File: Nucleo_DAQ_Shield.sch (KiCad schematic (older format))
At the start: 32 parts, among them J1 CONN_01X06, J2 CONN_01X06, J3 CONN_01X02, J4 CONN_01X02, J6 CONN_COAXIAL, J7 CONN_01X02, U1 4050, U10 ST_Nucleo144_F746ZG_CN10, U2 TL072, U3 LM7805CT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

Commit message: Added through hold Schottky diode as an alternative to SOD-123 Schottky diode
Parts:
- removed D1: D_Schottky, Diodes_SMD:D_SOD-123, symbol D_Schottky
- added D1: SD103 SOD-123, Diodes_SMD:D_SOD-123, symbol D_Schottky_Small
- added D3: SD103 DO-35, Diodes_THT:D_DO-35_SOD27_P7.62mm_Horizontal, symbol D_Schottky_Small
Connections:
- wire segments 48 -> 51
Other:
- note added: "Jumper enables overvoltage protection\n with the Schottky diode\nOnly solder one of the diodes shown"
- note removed: "Jumper enables overvoltage protection\n with the Schottky diode"
- moved on the sheet: J6, R1, R5, R6
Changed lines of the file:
@@
 L CONN_COAXIAL J6
 U 1 1 59542D8D
-P 5050 5900
-F 0 "J6" H 5060 6020 50  0000 C CNN
-F 1 "CONN_COAXIAL" V 5165 5900 50  0000 C CNN
-F 2 "custom:SMA_uxcell" H 5050 5900 50  0001 C CNN
-F 3 "" H 5050 5900 50  0001 C CNN
-	1    5050 5900
+P 4850 5900
+F 0 "J6" H 4860 6020 50  0000 C CNN
+F 1 "CONN_COAXIAL" V 4965 5900 50  0000 C CNN
+F 2 "custom:SMA_uxcell" H 4850 5900 50  0001 C CNN
+F 3 "" H 4850 5900 50  0001 C CNN
+	1    4850 5900
 	-1   0    0    -1
 $EndComp
@@
 L GNDA #PWR010
 U 1 1 59543B89
-P 5050 6100
-F 0 "#PWR010" H 5050 5850 50  0001 C CNN
-F 1 "GNDA" H 5050 5950 50  0000 C CNN
-F 2 "" H 5050 6100 50  0001 C CNN
-F 3 "" H 5050 6100 50  0001 C CNN
-	1    5050 6100
+P 4850 6100
+F 0 "#PWR010" H 4850 5850 50  0001 C CNN
+F 1 "GNDA" H 4850 5950 50  0000 C CNN
+F 2 "" H 4850 6100 50  0001 C CNN
+F 3 "" H 4850 6100 50  0001 C CNN
+	1    4850 6100
 	1    0    0    -1
 $EndComp
@@
 Nucleo connectors
 $Comp
-L D_Schottky D1
-U 1 1 595D9361
-P 6100 5650
-F 0 "D1" H 6100 5750 50  0000 C CNN
-F 1 "D_Schottky" H 6100 5550 50  0000 C CNN
-F 2 "Diodes_SMD:D_SOD-123" H 6100 5650 50  0001 C CNN
-F 3 "" H 6100 5650 50  0001 C CNN
-	1    6100 5650
-	0    1    1    0
-$EndComp
-$Comp
 L Jumper_NC_Small JP3
 U 1 1 595D9DFC
@@
 L R_Small R1
 U 1 1 595DA3C3
-P 5800 5900
-F 0 "R1" H 5830 5920 50  0000 L CNN
-F 1 "100" H 5830 5860 50  0000 L CNN
-F 2 "Resistors_SMD:R_0805" H 5800 5900 50  0001 C CNN
-F 3 "" H 5800 5900 50  0001 C CNN
-	1    5800 5900
+P 5600 5900
+F 0 "R1" H 5630 5920 50  0000 L CNN
+F 1 "100" H 5630 5860 50  0000 L CNN
+F 2 "Resistors_SMD:R_0805" H 5600 5900 50  0001 C CNN
+F 3 "" H 5600 5900 50  0001 C CNN
+	1    5600 5900
 	0    1    1    0
 $EndComp
 Text Notes 5650 5350 0    30   ~ 0
-Jumper enables overvoltage protection\n with the Schottky diode
+Jumper enables overvoltage protection\n with the Schottky diode\nOnly solder one of the diodes shown
 Text Notes 750  2050 0    60   ~ 0
 Motor and encoder interface
-Text Notes 5200 6350 0    30   ~ 0
+Text Notes 5000 6350 0    30   ~ 0
 50 Ohm termination resistor
 Text Notes 1800 3650 0    30   ~ 0
@@
 	600  5100 600  2100
 Wire Notes Line
-	4800 6500 4800 5200
-Wire Wire Line
-	5200 5900 5700 5900
-Connection ~ 6100 5900
-Wire Wire Line
-	6100 5800 6100 5900
-Wire Wire Line
-	5900 5900 6500 5900
-Wire Wire Line
-	6100 5500 6300 5500
+	4600 6500 4600 5200
+Wire Wire Line
+	5000 5900 5500 5900
+Wire Wire Line
+	5700 5900 6500 5900
 Connection ~ 6700 5500
 Wire Wire Line
@@
 Connection ~ 2100 1000
 Wire Notes Line
-	4800 6500 8200 6500
+	4600 6500 8200 6500
 Wire Notes Line
 	8200 6500 8200 5200
 Wire Notes Line
-	8200 5200 4800 5200
+	8200 5200 4600 5200
 Connection ~ 7200 6000
 Wire Notes Line
@@
 L R_Small R6
 U 1 1 59654171
-P 5600 6000
-F 0 "R6" H 5630 6020 50  0000 L CNN
-F 1 "100" H 5630 5960 50  0000 L CNN
-F 2 "Resistors_SMD:R_0805" H 5600 6000 50  0001 C CNN
-F 3 "" H 5600 6000 50  0001 C CNN
-	1    5600 6000
-	-1   0    0    1
-$EndComp
-$Comp
-L R_Small R5
-U 1 1 596541F7
 P 5400 6000
-F 0 "R5" H 5430 6020 50  0000 L CNN
+F 0 "R6" H 5430 6020 50  0000 L CNN
 F 1 "100" H 5430 5960 50  0000 L CNN
 F 2 "Resistors_SMD:R_0805" H 5400 6000 50  0001 C CNN
@@
 $EndComp
 $Comp
+L R_Small R5
+U 1 1 596541F7
+P 5200 6000
+F 0 "R5" H 5230 6020 50  0000 L CNN
+F 1 "100" H 5230 5960 50  0000 L CNN
+F 2 "Resistors_SMD:R_0805" H 5200 6000 50  0001 C CNN
+F 3 "" H 5200 6000 50  0001 C CNN
+	1    5200 6000
+	-1   0    0    1
+$EndComp
+$Comp
 L GNDA #PWR048
 U 1 1 5965449B
-P 5600 6100
-F 0 "#PWR048" H 5600 5850 50  0001 C CNN
-F 1 "GNDA" H 5600 5950 50  0000 C CNN
-F 2 "" H 5600 6100 50  0001 C CNN
-F 3 "" H 5600 6100 50  0001 C CNN
-	1    5600 6100
-	1    0    0    -1
-$EndComp
-$Comp
-L GNDA #PWR049
-U 1 1 59654512
 P 5400 6100
-F 0 "#PWR049" H 5400 5850 50  0001 C CNN
+F 0 "#PWR048" H 5400 5850 50  0001 C CNN
 F 1 "GNDA" H 5400 5950 50  0000 C CNN
 F 2 "" H 5400 6100 50  0001 C CNN
@@
 	1    0    0    -1
 $EndComp
-Connection ~ 5600 5900
+$Comp
+L GNDA #PWR049
+U 1 1 59654512
+P 5200 6100
+F 0 "#PWR049" H 5200 5850 50  0001 C CNN
+F 1 "GNDA" H 5200 5950 50  0000 C CNN
+F 2 "" H 5200 6100 50  0001 C CNN
+F 3 "" H 5200 6100 50  0001 C CNN
+	1    5200 6100
+	1    0    0    -1
+$EndComp
 Connection ~ 5400 5900
+Connection ~ 5200 5900
 NoConn ~ 6700 1100
 NoConn ~ 6700 1200
@@
 NoConn ~ 10200 4200
 NoConn ~ 1100 4000
-Text Notes 5000 5700 0    30   ~ 0
+Text Notes 4800 5700 0    30   ~ 0
 SMA connector
 $Comp
@@
 	1    0    0    -1
 $EndComp
+$Comp
+L D_Schottky_Small D1
+U 1 1 5965AAB6
+P 6150 5700
+F 0 "D1" H 6100 5780 50  0000 L CNN
+F 1 "SD103 SOD-123" H 5870 5620 30  0000 L CNN
+F 2 "Diodes_SMD:D_SOD-123" V 6150 5700 50  0001 C CNN
+F 3 "" V 6150 5700 50  0001 C CNN
+	1    6150 5700
+	0    1    1    0
+$EndComp
+Wire Wire Line
+	6150 5800 6150 5900
+Connection ~ 6150 5900
+Wire Wire Line
+	6150 5600 6150 5500
+Wire Wire Line
+	5900 5500 6300 5500
+$Comp
+L D_Schottky_Small D3
+U 1 1 5965B94C
+P 5900 5700
+F 0 "D3" H 5850 5780 50  0000 L CNN
+F 1 "SD103 DO-35" H 5620 5620 30  0000 L CNN
+F 2 "Diodes_THT:D_DO-35_SOD27_P7.62mm_Horizontal" V 5900 5700 50  0001 C CNN
+F 3 "" V 5900 5700 50  0001 C CNN
+	1    5900 5700
+	0    1    1    0
+$EndComp
+Wire Wire Line
+	5900 5600 5900 5500
+Connection ~ 6150 5500
+Wire Wire Line
+	5900 5800 5900 5900
+Connection ~ 5900 5900
 $EndSCHEMATC

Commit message: Nucleo DAQ Shield v1.2
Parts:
- U3: value LM7805CT -> L78L05
- U5: footprint Housings_SOIC:SOIC-8_3.9x4.9mm_Pitch1.27mm -> custom:SOIC-8_PowerPad
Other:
- note added: "3.3V 300mA regulator\nSOT-23-5 package"
- note added: "5V LDO regulator 100mA\nTO-92 package"
- note removed: "3.3V 300mA regulator"
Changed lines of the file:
@@
 Title "Nucleo DAQ Shield"
 Date "2017-07-11"
-Rev "v1.0"
+Rev "v1.2"
 Comp "Columbia University - Creative Machines Lab"
 Comment1 ""
@@
 Vbat
 Text Notes 5100 800  0    30   ~ 0
-3.3V 300mA regulator
+3.3V 300mA regulator\nSOT-23-5 package
 $Comp
 L GND #PWR019
@@
 F 0 "U5" H 4900 4025 60  0000 C CNN
 F 1 "DRV8881" H 4900 3900 60  0000 C CNN
-F 2 "Housings_SOIC:SOIC-8_3.9x4.9mm_Pitch1.27mm" H 4900 3550 60  0001 C CNN
+F 2 "custom:SOIC-8_PowerPad" H 4900 3550 60  0001 C CNN
 F 3 "" H 4900 3550 60  0001 C CNN
 	1    4900 3550
@@
 P 3200 1050
 F 0 "U3" H 3000 1250 50  0000 C CNN
-F 1 "LM7805CT" H 3200 1250 50  0000 L CNN
+F 1 "L78L05" H 3200 1250 50  0000 L CNN
 F 2 "TO_SOT_Packages_THT:TO-92_Inline_Narrow_Oval" H 3200 1150 50  0001 C CIN
 F 3 "" H 3200 1050 50  0001 C CNN
@@
 	5900 5800 5900 5900
 Connection ~ 5900 5900
+Text Notes 2950 800  0    30   ~ 0
+5V LDO regulator 100mA\nTO-92 package
 $EndSCHEMATC

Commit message: Swapped out TO-92 footprint to make it larger; refined separation between AGND and DGND
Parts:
- U3: footprint TO_SOT_Packages_THT:TO-92_Inline_Narrow_Oval -> TO_SOT_Packages_THT:TO-92_Inline_Wide
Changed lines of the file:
@@
 F 0 "U3" H 3000 1250 50  0000 C CNN
 F 1 "L78L05" H 3200 1250 50  0000 L CNN
-F 2 "TO_SOT_Packages_THT:TO-92_Inline_Narrow_Oval" H 3200 1150 50  0001 C CIN
+F 2 "TO_SOT_Packages_THT:TO-92_Inline_Wide" H 3200 1150 50  0001 C CIN
 F 3 "" H 3200 1050 50  0001 C CNN
 	1    3200 1050

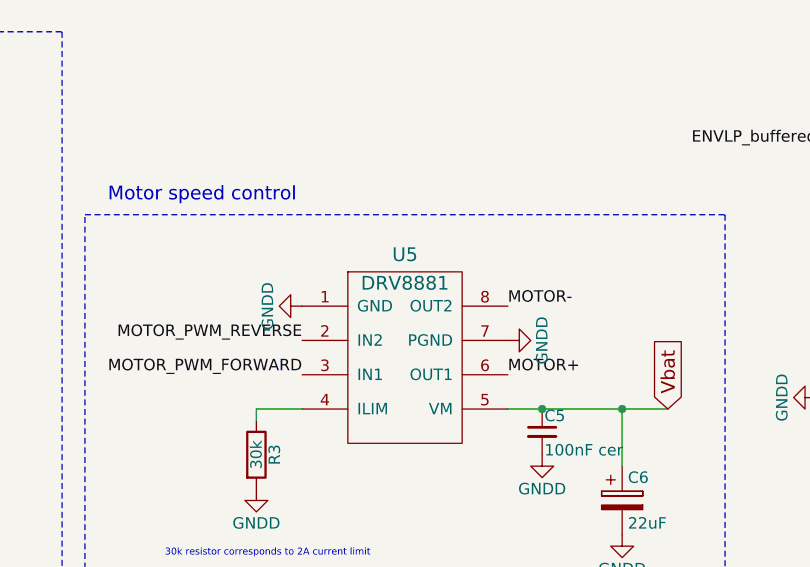
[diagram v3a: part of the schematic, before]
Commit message: BOM for Analog Frontend PCB v1.3
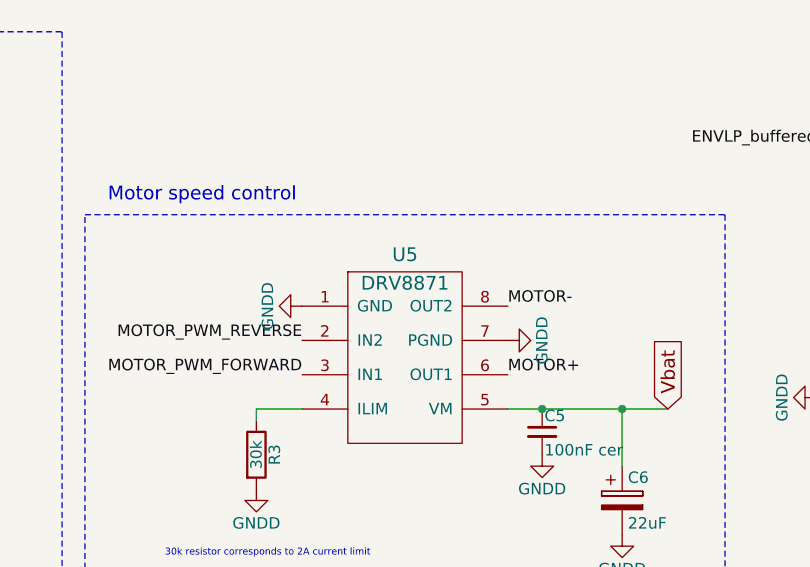
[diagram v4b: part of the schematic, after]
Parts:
- U5: value DRV8881 -> DRV8871
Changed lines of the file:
@@
 P 4900 3550
 F 0 "U5" H 4900 4025 60  0000 C CNN
-F 1 "DRV8881" H 4900 3900 60  0000 C CNN
+F 1 "DRV8871" H 4900 3900 60  0000 C CNN
 F 2 "custom:SOIC-8_PowerPad" H 4900 3550 60  0001 C CNN
 F 3 "" H 4900 3550 60  0001 C CNN

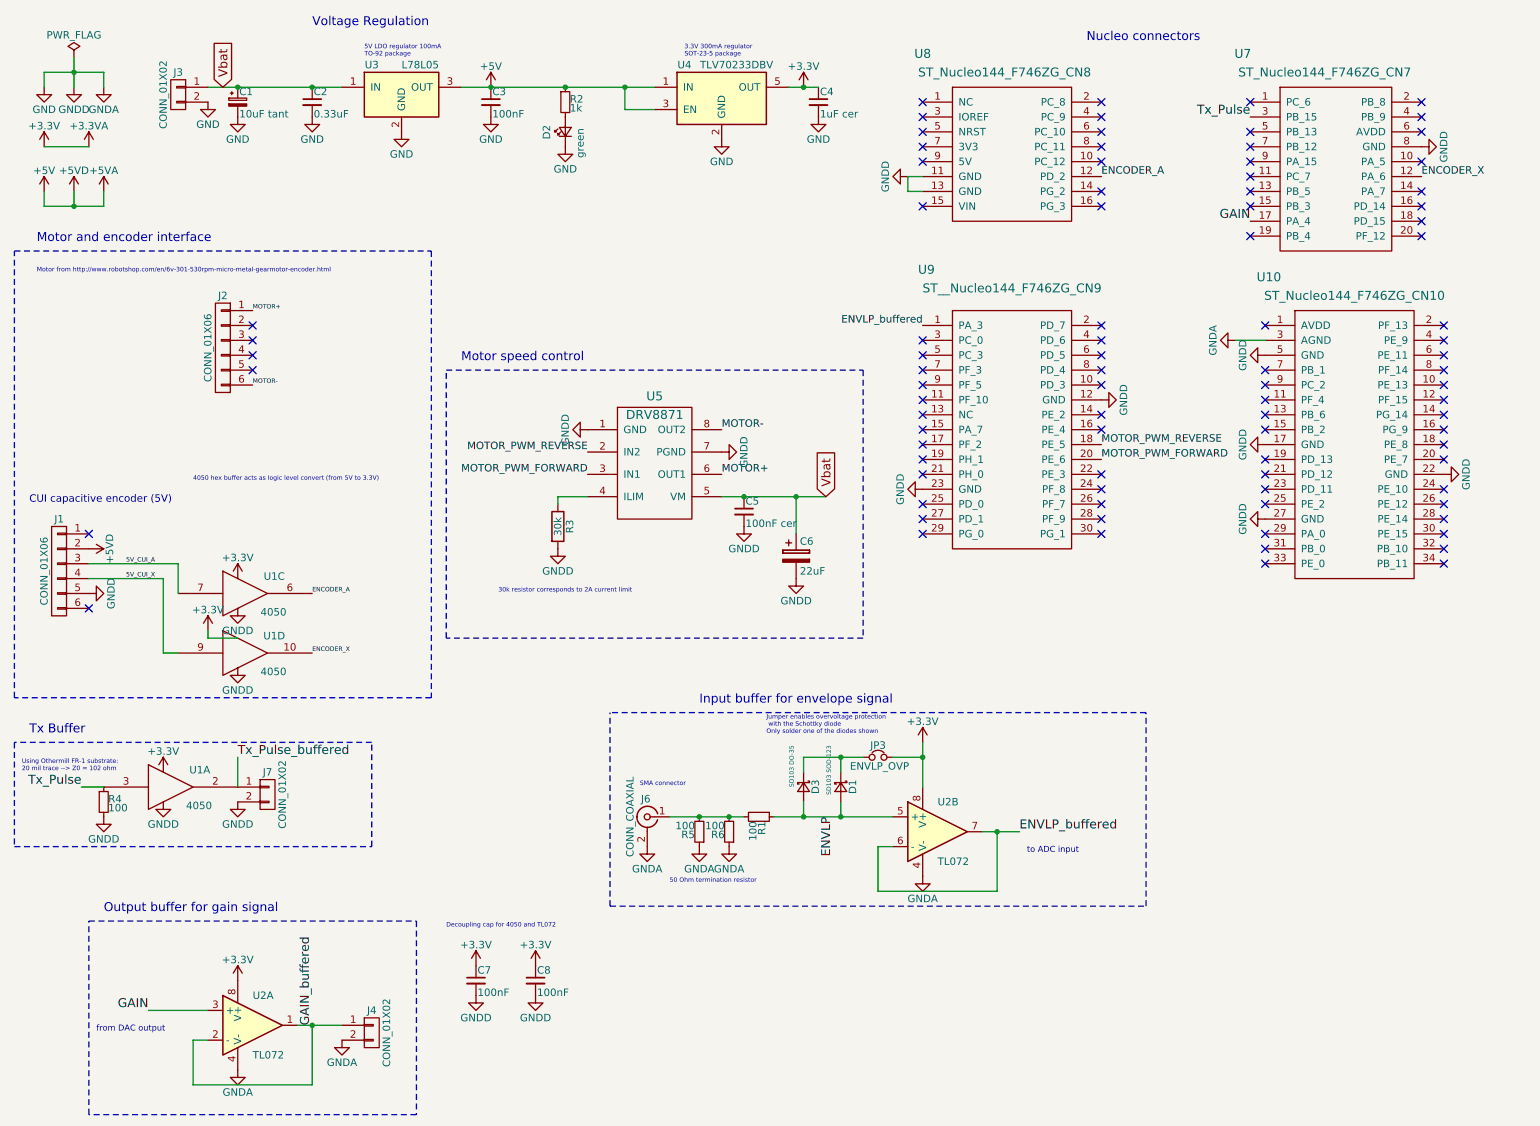
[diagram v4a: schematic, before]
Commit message: Analog BOM & Nucleo pins added
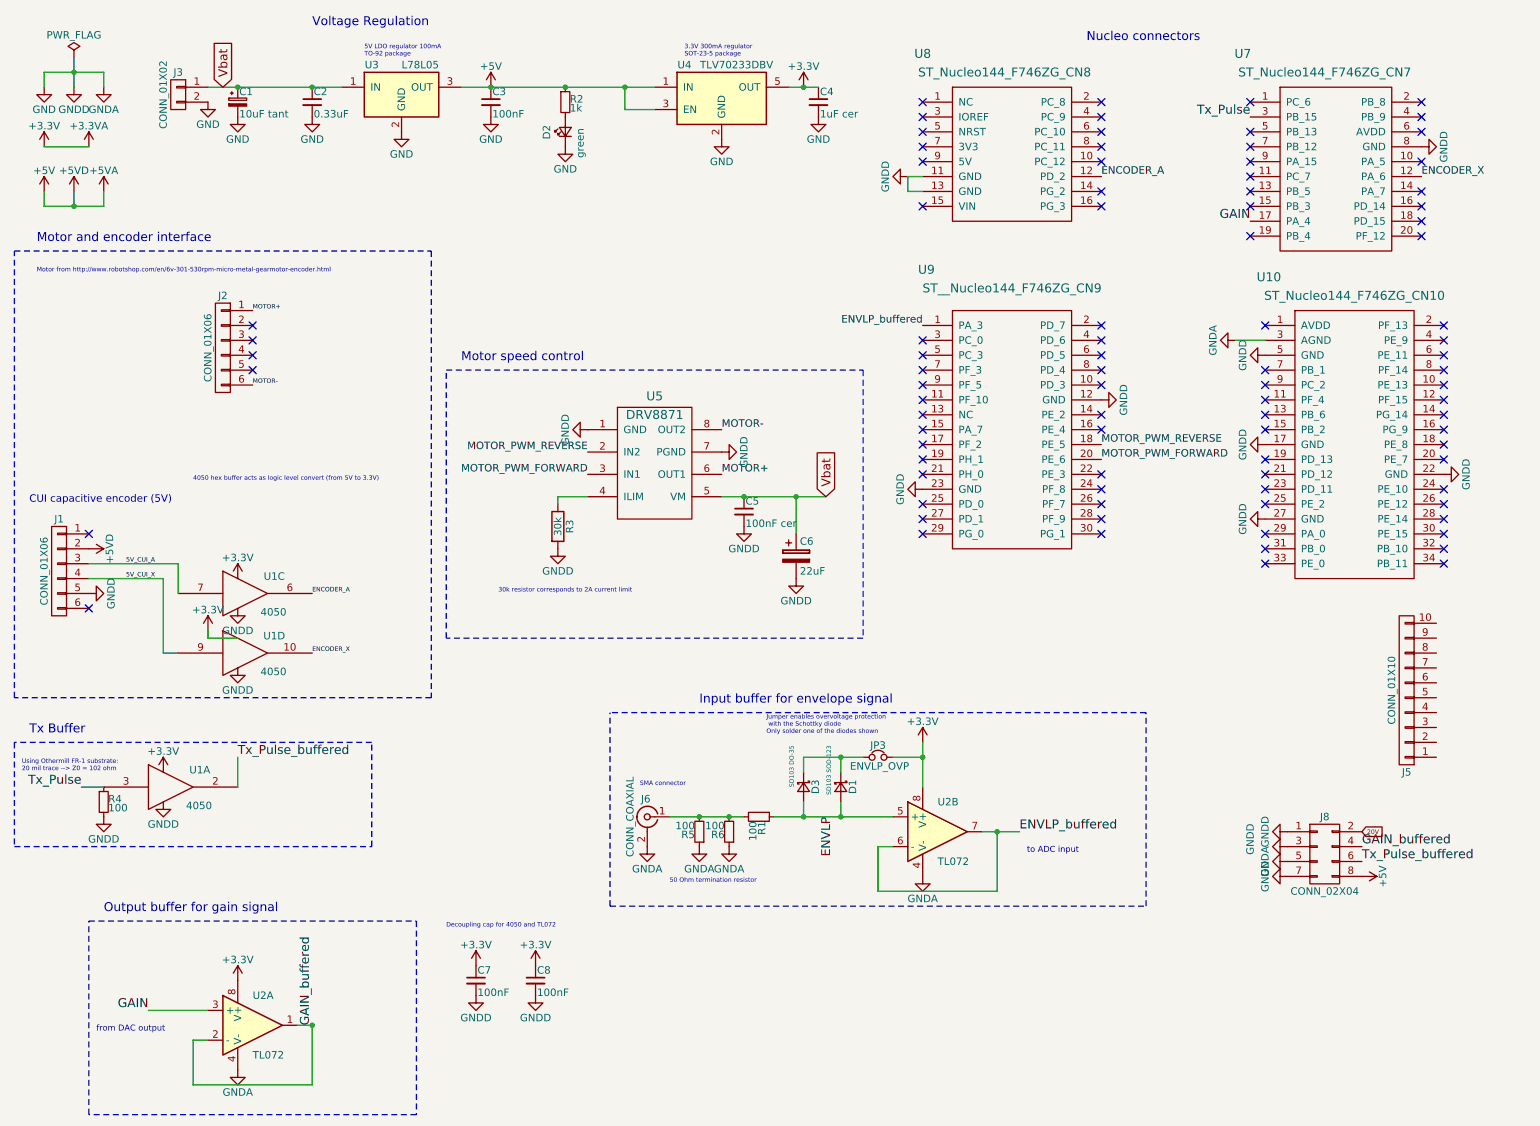
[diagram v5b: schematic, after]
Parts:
- removed J4, J7: CONN_01X02, Pin_Headers:Pin_Header_Straight_1x02_Pitch2.54mm, symbol CONN_01X02
- added J5: CONN_01X10, Pin_Headers:Pin_Header_Angled_1x10_Pitch2.54mm, symbol CONN_01X10
- added J8: CONN_02X04, Pin_Headers:Pin_Header_Straight_2x04_Pitch2.54mm, symbol CONN_02X04
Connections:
- net +5V: now also J8.8 (P8)
- net GAIN_buffered: now also J8.4 (P4)
- net GND: now also J8.1 (P1), J8.3 (P3), J8.5 (P5), J8.7 (P7)
- net Tx_Pulse_buffered: now also J8.6 (P6)
- new net 20V: J8.2 (P2)

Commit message: nucleo board updated
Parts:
- removed D3: SD103 DO-35, Diodes_THT:D_DO-35_SOD27_P7.62mm_Horizontal, symbol D_Schottky_Small
- removed J1: CONN_01X06, Pin_Headers:Pin_Header_Straight_1x06_Pitch2.54mm, symbol CONN_01X06
- added J1: CONN_01X05, Pin_Headers:Pin_Header_Straight_1x05_Pitch2.54mm, symbol CONN_01X05
- added J9: CONN_01X04, Pin_Headers:Pin_Header_Straight_1x04_Pitch2.54mm, symbol CONN_01X04
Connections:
- net +5V: now also J8.6 (P6), J1.4 (P4), J9.3 (P3); no longer J8.8 (P8)
- net 20V: now also J9.1 (P1)
- net 5V_CUI_A: now also J1.3 (P3)
- net 5V_CUI_X: now also J1.2 (P2)
- net GND: now also J1.1 (P1), J9.2 (P2), J9.4 (P4)
- net Tx_Pulse_buffered: now also J8.8 (P8); no longer J8.6 (P6)
- no-connect marks 89 -> 88
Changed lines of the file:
@@
 $EndComp
-$Comp
-L CONN_01X06 J1
-U 1 1 595D423B
-P 900 4250
-F 0 "J1" H 900 4600 50  0000 C CNN
-F 1 "CONN_01X06" V 1000 4250 50  0000 C CNN
-F 2 "Pin_Headers:Pin_Header_Straight_1x06_Pitch2.54mm" H 900 4250 50  0001 C CNN
-F 3 "" H 900 4250 50  0001 C CNN
-	1    900  4250
-	-1   0    0    -1
-$EndComp
-NoConn ~ 1100 4500
 $Comp
 L +5VD #PWR020
@@
 Wire Wire Line
 	6150 5600 6150 5500
-Wire Wire Line
-	5900 5500 6300 5500
-$Comp
-L D_Schottky_Small D3
-U 1 1 5965B94C
-P 5900 5700
-F 0 "D3" H 5850 5780 50  0000 L CNN
-F 1 "SD103 DO-35" H 5620 5620 30  0000 L CNN
-F 2 "Diodes_THT:D_DO-35_SOD27_P7.62mm_Horizontal" V 5900 5700 50  0001 C CNN
-F 3 "" V 5900 5700 50  0001 C CNN
-	1    5900 5700
-	0    1    1    0
-$EndComp
-Wire Wire Line
-	5900 5600 5900 5500
 Connection ~ 6150 5500
-Wire Wire Line
-	5900 5800 5900 5900
-Connection ~ 5900 5900
 Text Notes 2950 800  0    30   ~ 0
 5V LDO regulator 100mA\nTO-92 package
@@
 L +5V #PWR058
 U 1 1 59E8A941
-P 9650 6300
-F 0 "#PWR058" H 9650 6150 50  0001 C CNN
-F 1 "+5V" H 9650 6440 50  0000 C CNN
-F 2 "" H 9650 6300 50  0001 C CNN
-F 3 "" H 9650 6300 50  0001 C CNN
-	1    9650 6300
+P 9650 6200
+F 0 "#PWR058" H 9650 6050 50  0001 C CNN
+F 1 "+5V" H 9650 6340 50  0000 C CNN
+F 2 "" H 9650 6200 50  0001 C CNN
+F 3 "" H 9650 6200 50  0001 C CNN
+	1    9650 6200
 	0    1    1    0
 $EndComp
 Text GLabel 9650 6000 2    30   Input ~ 0
 20V
-Text Label 9650 6200 0    60   ~ 0
+Text Label 9650 6300 0    60   ~ 0
 Tx_Pulse_buffered
+Wire Wire Line
+	6150 5500 6300 5500
+$Comp
+L CONN_01X04 J9
+U 1 1 59EFD9C5
+P 8700 6200
+F 0 "J9" H 8700 6450 50  0000 C CNN
+F 1 "CONN_01X04" V 8800 6200 50  0000 C CNN
+F 2 "Pin_Headers:Pin_Header_Straight_1x04_Pitch2.54mm" H 8700 6200 50  0001 C CNN
+F 3 "" H 8700 6200 50  0001 C CNN
+	1    8700 6200
+	1    0    0    -1
+$EndComp
+Text GLabel 8500 6050 0    30   Input ~ 0
+20V
+$Comp
+L +5V #PWR059
+U 1 1 59EFDF5E
+P 8500 6250
+F 0 "#PWR059" H 8500 6100 50  0001 C CNN
+F 1 "+5V" H 8500 6390 50  0000 C CNN
+F 2 "" H 8500 6250 50  0001 C CNN
+F 3 "" H 8500 6250 50  0001 C CNN
+	1    8500 6250
+	0    -1   -1   0
+$EndComp
+$Comp
+L GNDD #PWR060
+U 1 1 59EFE046
+P 8500 6150
+F 0 "#PWR060" H 8500 5900 50  0001 C CNN
+F 1 "GNDD" H 8500 6000 50  0000 C CNN
+F 2 "" H 8500 6150 50  0001 C CNN
+F 3 "" H 8500 6150 50  0001 C CNN
+	1    8500 6150
+	0    1    1    0
+$EndComp
+$Comp
+L GNDD #PWR061
+U 1 1 59EFE0BD
+P 8500 6350
+F 0 "#PWR061" H 8500 6100 50  0001 C CNN
+F 1 "GNDD" H 8500 6200 50  0000 C CNN
+F 2 "" H 8500 6350 50  0001 C CNN
+F 3 "" H 8500 6350 50  0001 C CNN
+	1    8500 6350
+	0    1    1    0
+$EndComp
+$Comp
+L CONN_01X05 J1
+U 1 1 59EFF2B7
+P 900 4200
+F 0 "J1" H 900 4500 50  0000 C CNN
+F 1 "CONN_01X05" V 1000 4200 50  0000 C CNN
+F 2 "Pin_Headers:Pin_Header_Straight_1x05_Pitch2.54mm" H 900 4200 50  0001 C CNN
+F 3 "" H 900 4200 50  0001 C CNN
+	1    900  4200
+	-1   0    0    1
+$EndComp
 $EndSCHEMATC
